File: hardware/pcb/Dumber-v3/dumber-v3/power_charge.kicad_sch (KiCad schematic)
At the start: 44 parts, among them P1 USB_C_Plug_GCT_USB4125, Q1 PMN52XP, SW1 SW_Push, U3 LTC2954-2, U4 L6924U, U5 LM2731XMF, U6 AP2206

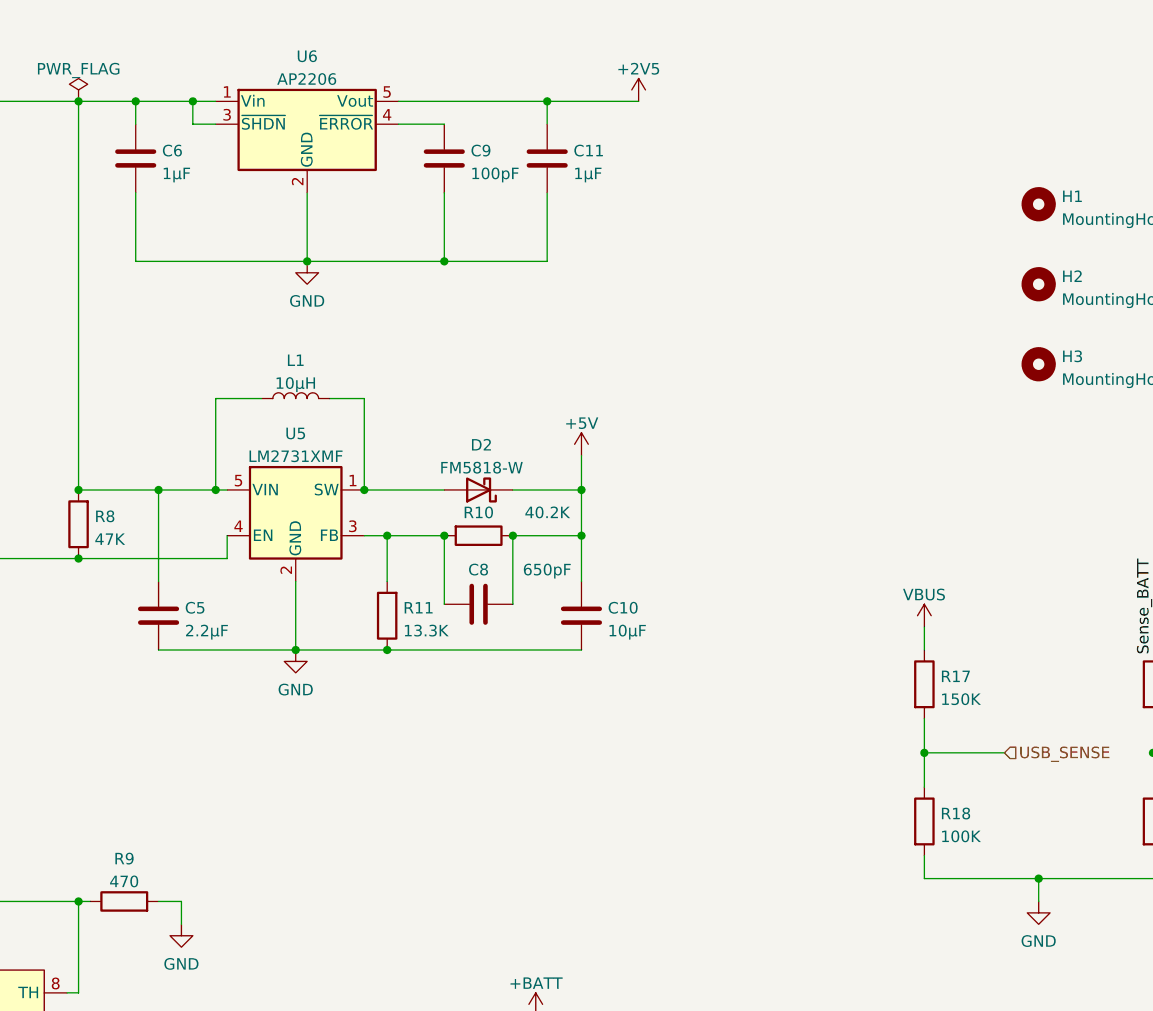
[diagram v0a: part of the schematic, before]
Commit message: Modifications after testing: func 11 needs more work.
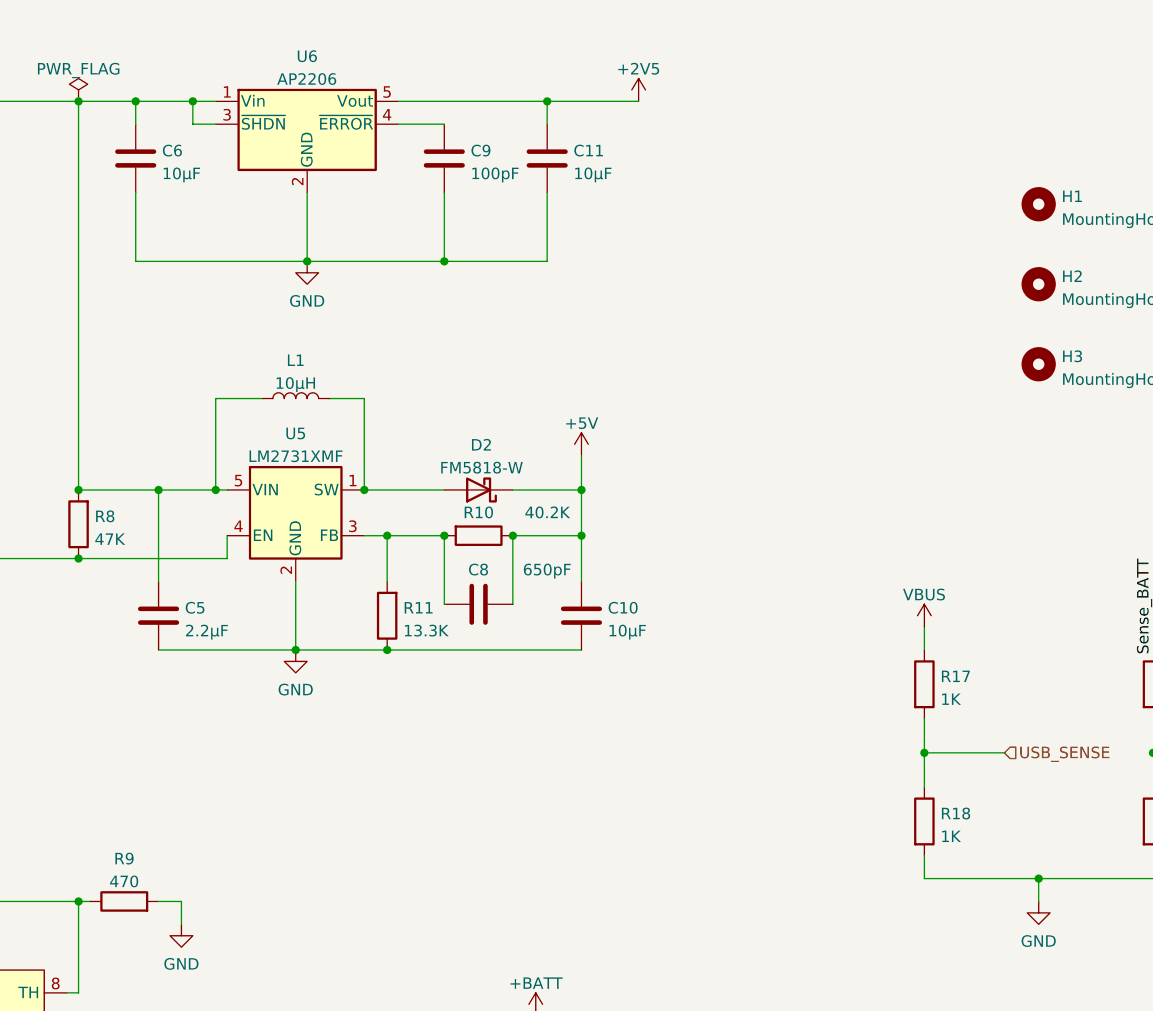
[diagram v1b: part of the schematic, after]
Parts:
- C11, C6: value 1µF -> 10µF
- R17: value 150K -> 1K
- R18: value 100K -> 1K
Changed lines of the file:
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@@
   (title_block
     (title "Power & Charge")
-    (date "2022-06-08")
-    (rev "1.1")
+    (date "2023-04-14")
+    (rev "2.1")
     (company "INSA - GEI")
   )
@@
       (effects (font (size 1.27 1.27)) (justify left))
     )
-    (property "Value" "150K" (id 1) (at 216.408 108.3822 0)
+    (property "Value" "1K" (id 1) (at 216.408 108.3822 0)
       (effects (font (size 1.27 1.27)) (justify left))
     )
@@
       (effects (font (size 1.27 1.27)) (justify left))
     )
-    (property "Value" "1µF" (id 1) (at 175.641 49.9622 0)
+    (property "Value" "10µF" (id 1) (at 175.641 49.9622 0)
       (effects (font (size 1.27 1.27)) (justify left))
     )
@@
       (effects (font (size 1.27 1.27)) (justify left))
     )
-    (property "Value" "1µF" (id 1) (at 129.921 49.9622 0)
+    (property "Value" "10µF" (id 1) (at 129.921 49.9622 0)
       (effects (font (size 1.27 1.27)) (justify left))
     )
@@
       (effects (font (size 1.27 1.27)) (justify left))
     )
-    (property "Value" "100K" (id 1) (at 216.408 123.6222 0)
-      (effects (font (size 1.27 1.27)) (justify left))
-    )
+    (property "Value" "1K" (id 1) (at 216.408 123.6222 0)
+      (effects (font (size 1.27 1.27)) (justify left))
+    )
